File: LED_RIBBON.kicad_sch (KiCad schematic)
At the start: 21 parts, among them J10 Conn_02x02_Odd_Even, J11 Conn_02x02_Odd_Even, J12 Conn_02x02_Odd_Even, J13 Conn_02x02_Odd_Even, J14 Conn_02x02_Odd_Even, J15 Conn_02x02_Odd_Even, J16 Conn_02x02_Odd_Even, J17 Conn_02x02_Odd_Even, U13 TCA9617A

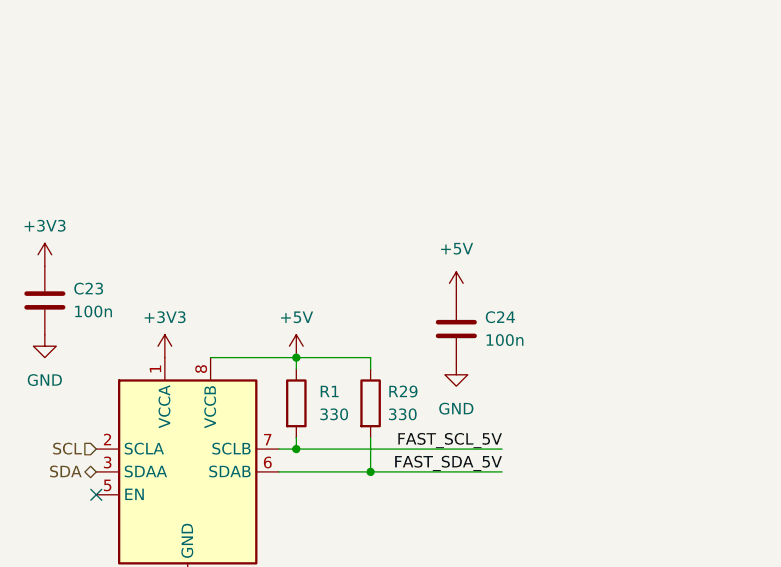
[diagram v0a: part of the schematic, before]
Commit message: switching to 3v3 i2c
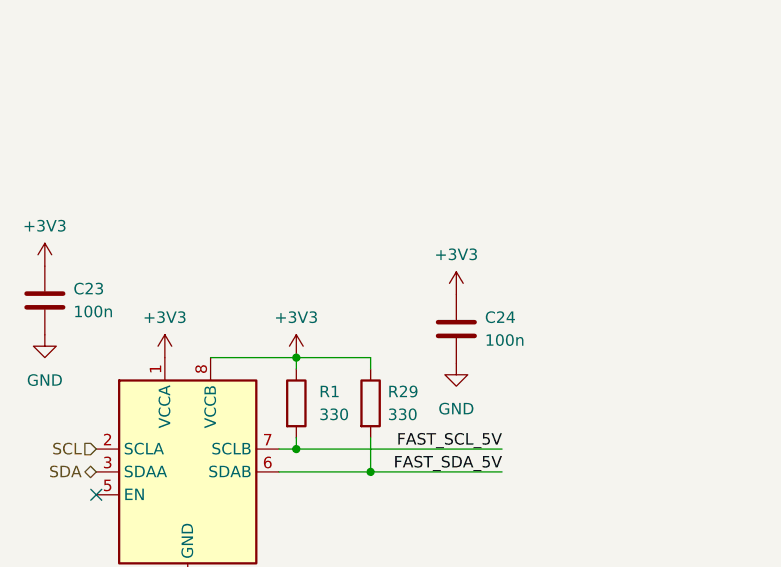
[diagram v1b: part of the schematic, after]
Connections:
- net +3V3: now also C24.1, R1.1, R29.1, U13.8 (VCCB)
- net +5V: no longer C24.1, R1.1, R29.1, U13.8 (VCCB)
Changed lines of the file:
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@@
-    )
-  )
-  (symbol (lib_id "power:+5V") (at 48.26 160.655 0) (unit 1)
-    (in_bom yes) (on_board yes) (dnp no) (fields_autoplaced)
-    (property "Reference" "#PWR029" (at 48.26 164.465 0)
-      (effects (font (size 1.27 1.27)) hide)
-    )
-    (property "Value" "+5V" (at 48.26 156.21 0)
-      (effects (font (size 1.27 1.27)))
-    )
-    (property "Footprint" "" (at 48.26 160.655 0)
-      (effects (font (size 1.27 1.27)) hide)
-    )
-    (property "Datasheet" "" (at 48.26 160.655 0)
-      (effects (font (size 1.27 1.27)) hide)
-    )
-    (pin "1")
-    (instances
-      (project "speedomobile"
-        (path "/33f5bcad-68ad-4ea6-9034-cdbd4086270c/b42eefb6-cfe9-4ab9-9135-cec9245263a5/5f6994f2-6ebc-4b96-a957-b36a33b2dc9e"
-          (reference "#PWR029") (unit 1)
-        )
-      )
     )
   )
@@
     )
   )
+  (symbol (lib_id "power:+3V3") (at 48.26 160.655 0) (unit 1)
+    (in_bom yes) (on_board yes) (dnp no) (fields_autoplaced)
+    (property "Reference" "#PWR029" (at 48.26 164.465 0)
+      (effects (font (size 1.27 1.27)) hide)
+    )
+    (property "Value" "+3V3" (at 48.26 156.21 0)
+      (effects (font (size 1.27 1.27)))
+    )
+    (property "Footprint" "" (at 48.26 160.655 0)
+      (effects (font (size 1.27 1.27)) hide)
+    )
+    (property "Datasheet" "" (at 48.26 160.655 0)
+      (effects (font (size 1.27 1.27)) hide)
+    )
+    (pin "1")
+    (instances
+      (project "speedomobile"
+        (path "/33f5bcad-68ad-4ea6-9034-cdbd4086270c/b42eefb6-cfe9-4ab9-9135-cec9245263a5/5f6994f2-6ebc-4b96-a957-b36a33b2dc9e"
+          (reference "#PWR029") (unit 1)
+        )
+      )
+    )
+  )
   (symbol (lib_id "power:GNDPWR") (at 156.845 60.96 0) (unit 1)
     (in_bom yes) (on_board yes) (dnp no) (fields_autoplaced)
@@
         (path "/33f5bcad-68ad-4ea6-9034-cdbd4086270c/b42eefb6-cfe9-4ab9-9135-cec9245263a5/5f6994f2-6ebc-4b96-a957-b36a33b2dc9e"
           (reference "#PWR034") (unit 1)
-        )
-      )
-    )
-  )
-  (symbol (lib_id "power:+5V") (at 66.04 153.67 0) (unit 1)
-    (in_bom yes) (on_board yes) (dnp no) (fields_autoplaced)
-    (property "Reference" "#PWR032" (at 66.04 157.48 0)
-      (effects (font (size 1.27 1.27)) hide)
-    )
-    (property "Value" "+5V" (at 66.04 148.59 0)
-      (effects (font (size 1.27 1.27)))
-    )
-    (property "Footprint" "" (at 66.04 153.67 0)
-      (effects (font (size 1.27 1.27)) hide)
-    )
-    (property "Datasheet" "" (at 66.04 153.67 0)
-      (effects (font (size 1.27 1.27)) hide)
-    )
-    (pin "1")
-    (instances
-      (project "speedomobile"
-        (path "/33f5bcad-68ad-4ea6-9034-cdbd4086270c/b42eefb6-cfe9-4ab9-9135-cec9245263a5/5f6994f2-6ebc-4b96-a957-b36a33b2dc9e"
-          (reference "#PWR032") (unit 1)
         )
       )
@@
         )
       )
+    )
+  )
+  (symbol (lib_id "power:+3V3") (at 66.04 153.67 0) (unit 1)
+    (in_bom yes) (on_board yes) (dnp no) (fields_autoplaced)
+    (property "Reference" "#PWR032" (at 66.04 157.48 0)
+      (effects (font (size 1.27 1.27)) hide)
+    )
+    (property "Value" "+3V3" (at 66.04 149.225 0)
+      (effects (font (size 1.27 1.27)))
+    )
+    (property "Footprint" "" (at 66.04 153.67 0)
+      (effects (font (size 1.27 1.27)) hide)
+    )
+    (property "Datasheet" "" (at 66.04 153.67 0)
+      (effects (font (size 1.27 1.27)) hide)
+    )
+    (pin "1")
+    (instances
+      (project "speedomobile"
+        (path "/33f5bcad-68ad-4ea6-9034-cdbd4086270c/b42eefb6-cfe9-4ab9-9135-cec9245263a5/5f6994f2-6ebc-4b96-a957-b36a33b2dc9e"
+          (reference "#PWR032") (unit 1)
+        )
+      )

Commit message: JLCJLCJLCJLC
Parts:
- added J36, J39: Conn_02x02_Odd_Even, Connector_Molex:Molex_Mini-Fit_Jr_5566-04A_2x02_P4.20mm_Vertical, symbol Connector_Generic:Conn_02x02_Odd_Even
- added TH? (x2): 7,5A, Resistor_SMD:R_1210_3225Metric, symbol Device:Thermistor_PTC
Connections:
- net +5V: now also TH?.2, TH?.2
- net FAST_SCL_5V: now also J36.1 (Pin_1), J39.1 (Pin_1)
- net FAST_SDA_5V: now also J36.3 (Pin_3), J39.3 (Pin_3)
- net GNDPWR: now also J36.4 (Pin_4), J39.4 (Pin_4)
- new net LED10: J39.2 (Pin_2), TH?.1
- new net LED9: J36.2 (Pin_2), TH?.1
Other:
- moved on the sheet: J10, J11, J12, J13, J14, J15, J16, J17, TH?

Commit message: Before flip
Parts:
- J10, J11, J12, J13, J14, J15, J16, J17, J36, J39: mouser (none) -> 649-10127820-0422PLF; mouser2 (none) -> 571-1586019-4
- R1, R29: mouser (none) -> 603-RT1206FRE07330RL
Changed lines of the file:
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@@
+      (effects (font (size 1.27 1.27)) hide)
+    )
+    (property "mouser" " 649-10127820-0422PLF " (at 96.52 52.07 0)
+      (effects (font (size 1.27 1.27)) hide)
+    )
+    (property "mouser2" " 571-1586019-4 " (at 96.52 52.07 0)
+      (effects (font (size 1.27 1.27)) hide)
+    )
+    (property "tme" "" (at 96.52 52.07 0)
       (effects (font (size 1.27 1.27)) hide)
     )
@@
       (effects (font (size 1.27 1.27)) hide)
     )
+    (property "mouser2" "" (at 85.725 81.28 0)
+      (effects (font (size 1.27 1.27)) hide)
+    )
     (pin "1")
     (pin "2")
@@
       (effects (font (size 1.27 1.27)) hide)
     )
+    (property "mouser2" "" (at 192.405 33.02 0)
+      (effects (font (size 1.27 1.27)) hide)
+    )
     (pin "1")
     (pin "2")
@@
       (effects (font (size 1.27 1.27)) hide)
     )
+    (property "mouser" " 649-10127820-0422PLF " (at 96.52 100.33 0)
+      (effects (font (size 1.27 1.27)) hide)
+    )
+    (property "mouser2" " 571-1586019-4 " (at 96.52 100.33 0)
+      (effects (font (size 1.27 1.27)) hide)
+    )
+    (property "tme" "" (at 96.52 100.33 0)
+      (effects (font (size 1.27 1.27)) hide)
+    )
     (pin "4")
     (pin "1")
@@
       (effects (font (size 1.27 1.27)) hide)
     )
+    (property "mouser2" "" (at 139.7 80.01 0)
+      (effects (font (size 1.27 1.27)) hide)
+    )
     (pin "1")
     (pin "2")
@@
       (effects (font (size 1.27 1.27)) hide)
     )
+    (property "mouser" " 649-10127820-0422PLF " (at 149.86 52.07 0)
+      (effects (font (size 1.27 1.27)) hide)
+    )
+    (property "mouser2" " 571-1586019-4 " (at 149.86 52.07 0)
+      (effects (font (size 1.27 1.27)) hide)
+    )
+    (property "tme" "" (at 149.86 52.07 0)
+      (effects (font (size 1.27 1.27)) hide)
+    )
     (pin "4")
     (pin "1")
@@
       (effects (font (size 1.27 1.27)) hide)
     )
+    (property "mouser2" "" (at 166.37 81.28 0)
+      (effects (font (size 1.27 1.27)) hide)
+    )
     (pin "1")
     (pin "2")
@@
       (effects (font (size 1.27 1.27)) hide)
     )
+    (property "mouser2" "" (at 193.675 80.01 0)
+      (effects (font (size 1.27 1.27)) hide)
+    )
     (pin "1")
     (pin "2")
@@
       (effects (font (size 1.27 1.27)) hide)
     )
+    (property "mouser2" "" (at 139.065 33.02 0)
+      (effects (font (size 1.27 1.27)) hide)
+    )
     (pin "1")
     (pin "2")
@@
       (effects (font (size 1.27 1.27)) hide)
     )
+    (property "mouser" " 649-10127820-0422PLF " (at 177.165 100.33 0)
+      (effects (font (size 1.27 1.27)) hide)
+    )
+    (property "mouser2" " 571-1586019-4 " (at 177.165 100.33 0)
+      (effects (font (size 1.27 1.27)) hide)
+    )
+    (property "tme" "" (at 177.165 100.33 0)
+      (effects (font (size 1.27 1.27)) hide)
+    )
     (pin "4")
     (pin "1")
@@
       (effects (font (size 1.27 1.27)) hide)
     )
+    (property "mouser2" "" (at 85.725 33.02 0)
+      (effects (font (size 1.27 1.27)) hide)
+    )
     (pin "1")
     (pin "2")
@@
       (effects (font (size 1.27 1.27)) hide)
     )
+    (property "mouser2" "" (at 20.32 154.305 0)
+      (effects (font (size 1.27 1.27)) hide)
+    )
     (pin "1")
     (pin "2")
@@
       (effects (font (size 1.27 1.27)) hide)
     )
+    (property "mouser2" "" (at 165.735 33.02 0)
+      (effects (font (size 1.27 1.27)) hide)
+    )
     (pin "1")
     (pin "2")
@@
       (effects (font (size 1.27 1.27)) hide)
     )
+    (property "mouser" " 649-10127820-0422PLF " (at 150.495 100.33 0)
+      (effects (font (size 1.27 1.27)) hide)
+    )
+    (property "mouser2" " 571-1586019-4 " (at 150.495 100.33 0)
+      (effects (font (size 1.27 1.27)) hide)
+    )
+    (property "tme" "" (at 150.495 100.33 0)
+      (effects (font (size 1.27 1.27)) hide)
+    )
     (pin "4")
     (pin "1")
@@
     )
     (property "Datasheet" "~" (at 123.19 100.33 0)
+      (effects (font (size 1.27 1.27)) hide)
+    )
+    (property "mouser" " 649-10127820-0422PLF " (at 123.19 100.33 0)
+      (effects (font (size 1.27 1.27)) hide)
+    )
+    (property "mouser2" " 571-1586019-4 " (at 123.19 100.33 0)
+      (effects (font (size 1.27 1.27)) hide)
+    )
+    (property "tme" "" (at 123.19 100.33 0)
       (effects (font (size 1.27 1.27)) hide)
     )
@@
       (effects (font (size 1.27 1.27)) hide)
     )
+    (property "mouser2" "" (at 112.395 81.28 0)
+      (effects (font (size 1.27 1.27)) hide)
+    )
     (pin "1")
     (pin "2")
@@
       (effects (font (size 1.27 1.27)) hide)
     )
+    (property "mouser" " 649-10127820-0422PLF " (at 176.53 52.07 0)
+      (effects (font (size 1.27 1.27)) hide)
+    )
+    (property "mouser2" " 571-1586019-4 " (at 176.53 52.07 0)
+      (effects (font (size 1.27 1.27)) hide)
+    )
+    (property "tme" "" (at 176.53 52.07 0)
+      (effects (font (size 1.27 1.27)) hide)
+    )
     (pin "4")
     (pin "1")
@@
     )
     (property "Datasheet" "~" (at 123.19 52.07 0)
+      (effects (font (size 1.27 1.27)) hide)
+    )
+    (property "mouser" " 649-10127820-0422PLF " (at 123.19 52.07 0)
+      (effects (font (size 1.27 1.27)) hide)
+    )
+    (property "mouser2" " 571-1586019-4 " (at 123.19 52.07 0)
+      (effects (font (size 1.27 1.27)) hide)
+    )
+    (property "tme" "" (at 123.19 52.07 0)
       (effects (font (size 1.27 1.27)) hide)
     )
@@
       (effects (font (size 1.27 1.27)) hide)
     )
+    (property "mouser2" "" (at 66.04 157.48 0)
+      (effects (font (size 1.27 1.27)) hide)
+    )
     (pin "1")
     (pin "2")
@@
     )
     (property "mouser" " 595-TCA9617ADGKR " (at 36.195 173.355 0)
+      (effects (font (size 1.27 1.27)) hide)
+    )
+    (property "mouser2" "" (at 36.195 173.355 0)
       (effects (font (size 1.27 1.27)) hide)
     )
@@
       (effects (font (size 1.27 1.27)) hide)
     )
+    (property "mouser2" "" (at 48.26 165.735 0)
+      (effects (font (size 1.27 1.27)) hide)
+    )
+    (property "mouser" " 603-RT1206FRE07330RL " (at 48.26 165.735 0)
+      (effects (font (size 1.27 1.27)) hide)
+    )
     (pin "2")
     (pin "1")
@@
       (effects (font (size 1.27 1.27)) hide)
     )
+    (property "mouser" " 649-10127820-0422PLF " (at 204.47 100.33 0)
+      (effects (font (size 1.27 1.27)) hide)
+    )
+    (property "mouser2" " 571-1586019-4 " (at 204.47 100.33 0)
+      (effects (font (size 1.27 1.27)) hide)
+    )
+    (property "tme" "" (at 204.47 100.33 0)
+      (effects (font (size 1.27 1.27)) hide)
+    )
     (pin "4")
     (pin "1")
@@
       (effects (font (size 1.27 1.27)) hide)
     )
+    (property "mouser2" "" (at 112.395 33.02 0)
+      (effects (font (size 1.27 1.27)) hide)
+    )
     (pin "1")
     (pin "2")
@@
       (effects (font (size 1.27 1.27)) hide)
     )
+    (property "mouser" " 649-10127820-0422PLF " (at 203.2 52.07 0)
+      (effects (font (size 1.27 1.27)) hide)
+    )
+    (property "mouser2" " 571-1586019-4 " (at 203.2 52.07 0)
+      (effects (font (size 1.27 1.27)) hide)
+    )
+    (property "tme" "" (at 203.2 52.07 0)
+      (effects (font (size 1.27 1.27)) hide)
+    )
     (pin "4")
     (pin "1")
@@
       (effects (font (size 1.27 1.27)) hide)
     )
+    (property "mouser2" "" (at 56.515 165.735 0)
+      (effects (font (size 1.27 1.27)) hide)
+    )
+    (property "mouser" " 603-RT1206FRE07330RL " (at 56.515 165.735 0)
+      (effects (font (size 1.27 1.27)) hide)
+    )
